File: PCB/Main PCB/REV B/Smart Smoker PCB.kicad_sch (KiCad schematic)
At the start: 70 parts, among them J1 393570002, J3 1051330001, J4 MJ-3502, J7 Hopper, J8 Lid, Q1 25V 1.5A Trans, Q2 25V 1.5A Trans, U1 ESP32-WROOM-32UE_16MB, U2 DG409LEDY-T1-GE3, U3 MAX31855KASA, U4 CP2102N-Axx-xQFN20

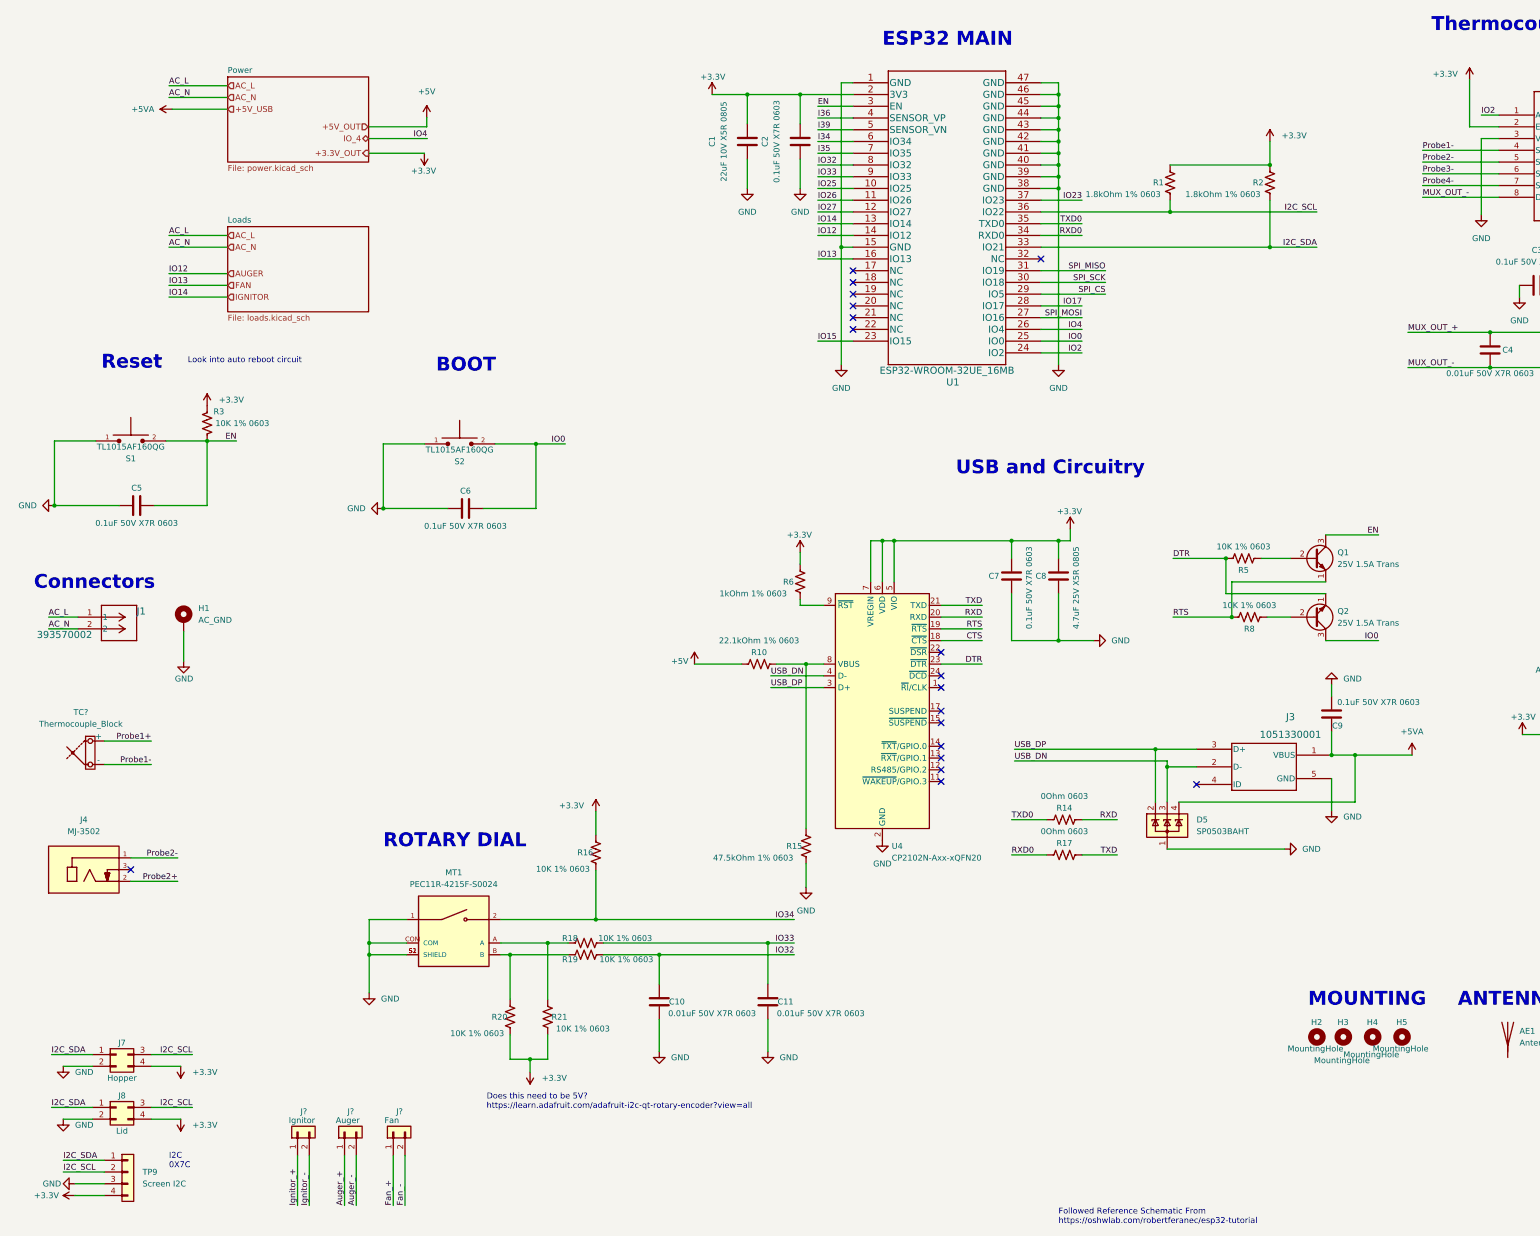
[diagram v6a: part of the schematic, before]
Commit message: PCB schematic updates, Screen and Probe jack updates
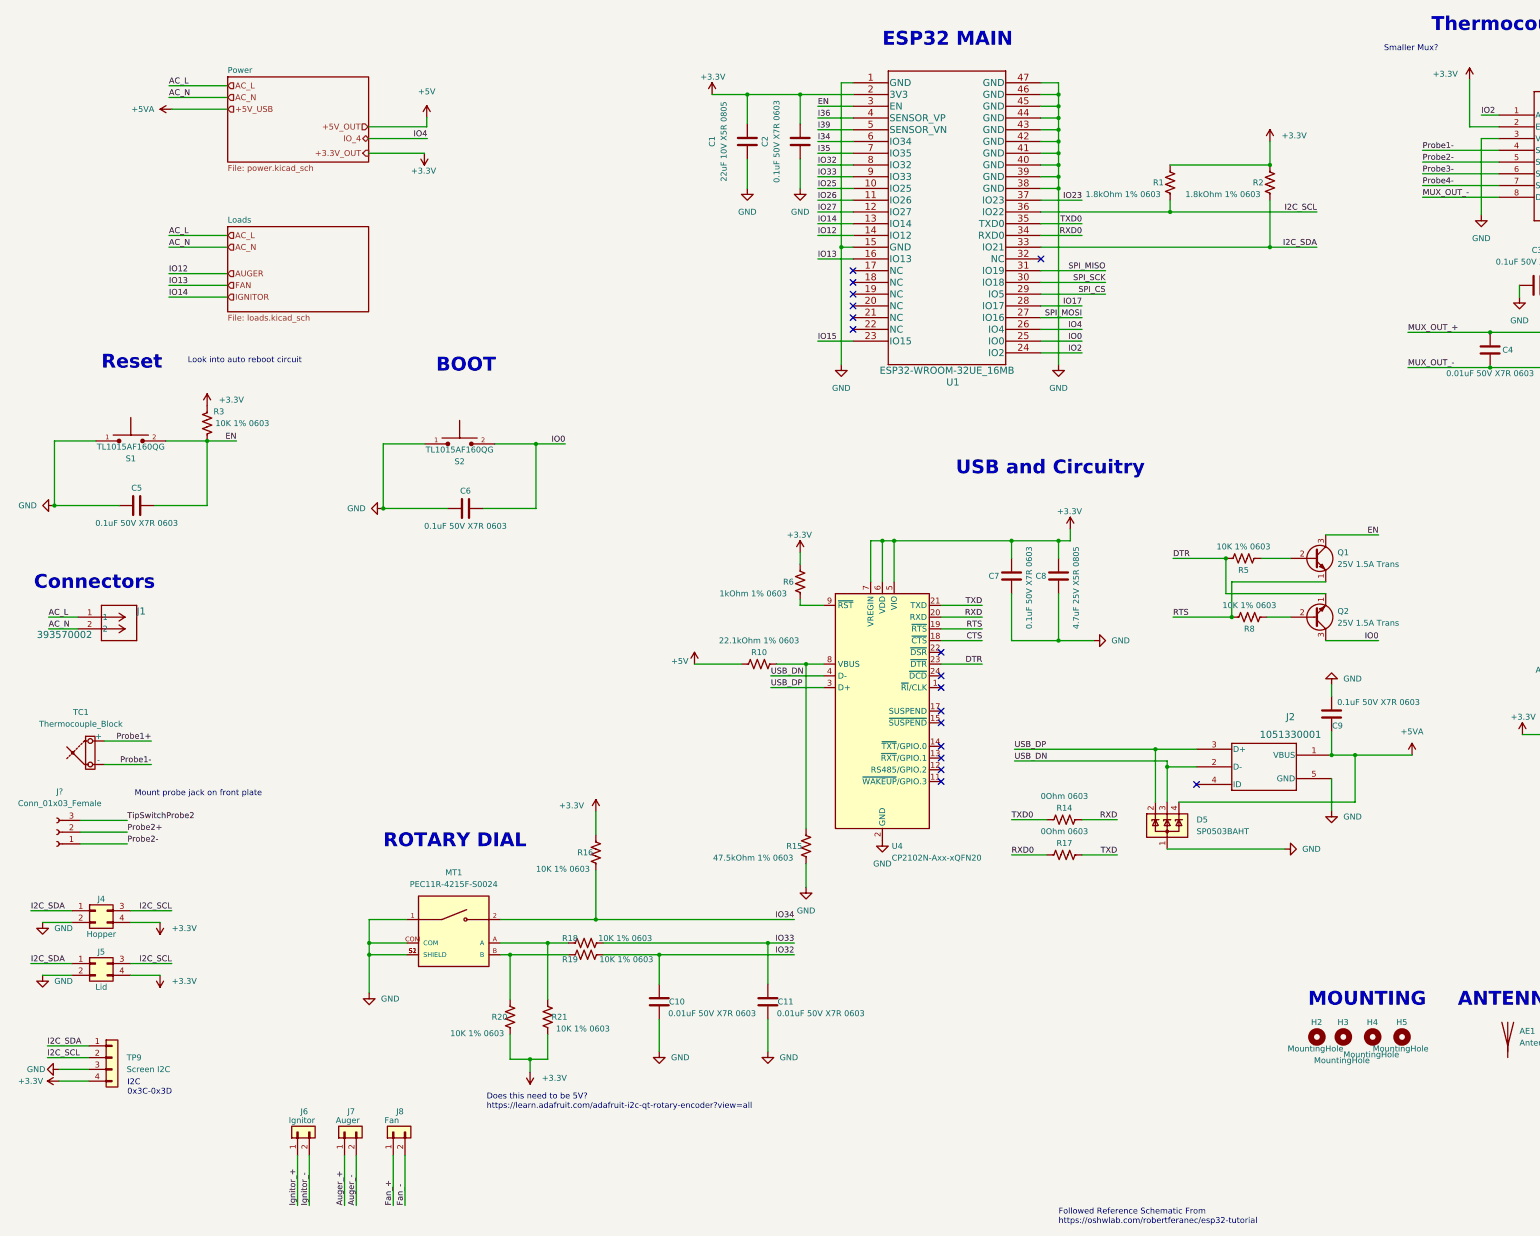
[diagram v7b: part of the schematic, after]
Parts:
- removed H1: AC_GND, MountingHole:MountingHole_3.2mm_M3_Pad_Via, symbol Mechanical:MountingHole_Pad
- removed J4: MJ-3502, Customs Smoker:CUI_MJ-3502, symbol MJ-3502:MJ-3502
- added J?: Conn_01x03_Female, Connector_PinHeader_2.54mm:PinHeader_1x03_P2.54mm_Vertical, symbol Connector:Conn_01x03_Female
- TP9: Manufacturer DFRobot -> Adafruit Industries LLC; Manufacturer Part Number DFR0555 -> 938; Vendor Part Number 1738-1411-ND -> 1528-1512-ND
- gave numbers to parts that had none: 4
- renumbered J3 to J2, J7 to J4, J8 to J5
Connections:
- net Probe2+: now also J?.2 (Pin_2)
- net Probe2-: now also J?.1 (Pin_1)
- new net TipSwitchProbe2: J?.3 (Pin_3)
- no-connect marks 18 -> 17
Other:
- note added: "I2C 0x3C-0x3D"
- note added: "Mount probe jack on front plate"
- note added: "Smaller Mux?"
- note removed: "I2C 0X7C"
- moved on the sheet: J4, J5, TP9

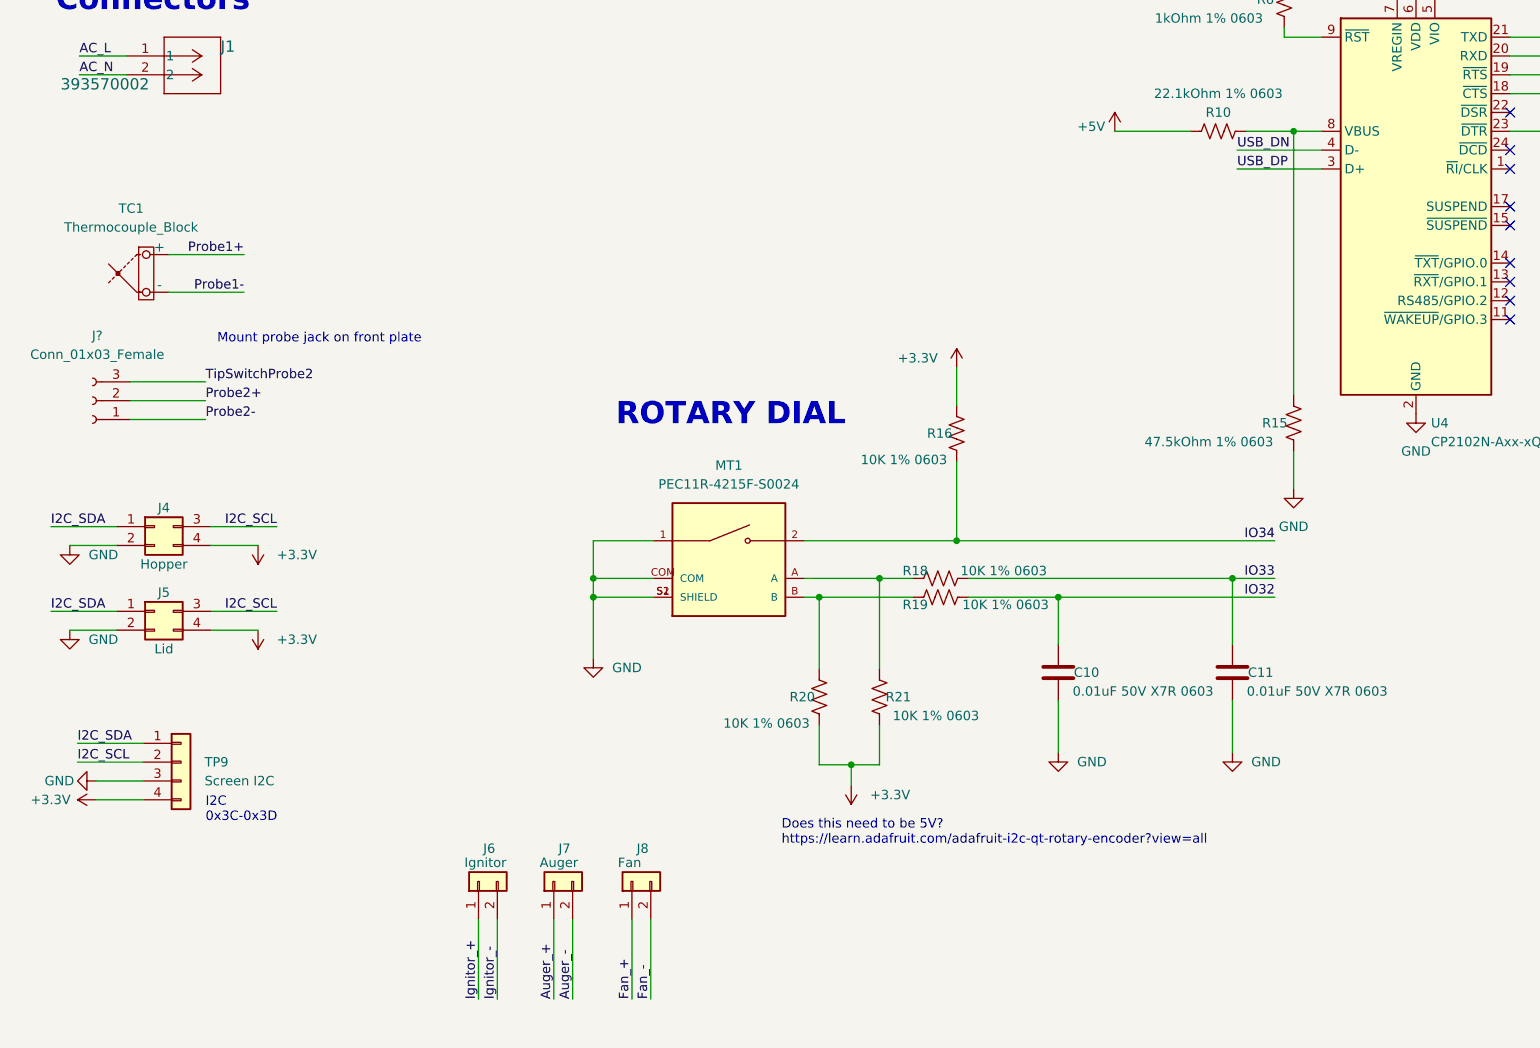
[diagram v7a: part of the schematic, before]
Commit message: PCB schematic updates, Rotary Encoder Updates
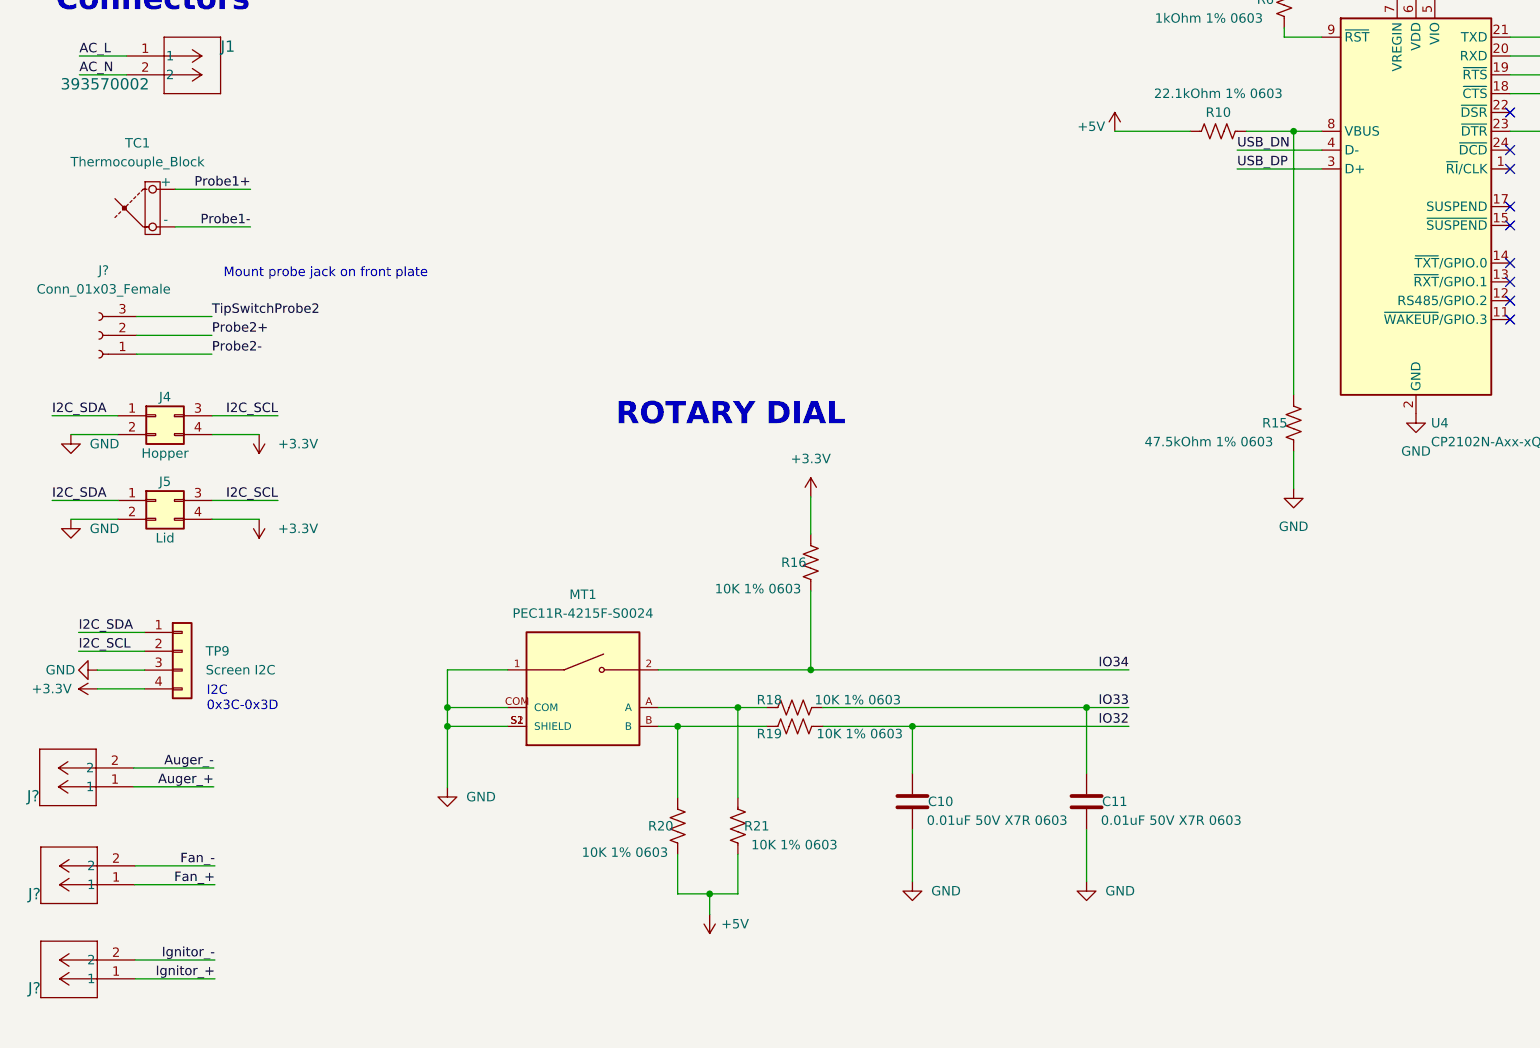
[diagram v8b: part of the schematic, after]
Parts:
- removed J6: Ignitor, TestPoint:TestPoint_2Pads_Pitch5.08mm_Drill1.3mm, symbol Connector_Generic:Conn_01x02
- removed J7: Auger, TestPoint:TestPoint_2Pads_Pitch5.08mm_Drill1.3mm, symbol Connector_Generic:Conn_01x02
- removed J8: Fan, TestPoint:TestPoint_2Pads_Pitch5.08mm_Drill1.3mm, symbol Connector_Generic:Conn_01x02
- added J? (x3): 393570002, CONN_393570002_MOL, symbol 0393570002:393570002
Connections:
- net +3.3V: no longer R20.1, R21.1
- net +5V: now also R20.1, R21.1
- net Auger_+: now also J?.1
- net Auger_-: now also J?.2
- net Fan_+: now also J?.1
- net Fan_-: now also J?.2
- net Ignitor_+: now also J?.1
- net Ignitor_-: now also J?.2
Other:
- note removed: "Does this need to be 5V? https://learn.adafruit.com/adafruit-i2c-qt-rotary-encoder?view=all"
- moved on the sheet: C10, C11, J4, J5, J?, MT1, R16, R18, R19, R20, R21, TC1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
